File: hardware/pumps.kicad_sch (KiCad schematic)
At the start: 14 parts, among them Q5 BUK6D210

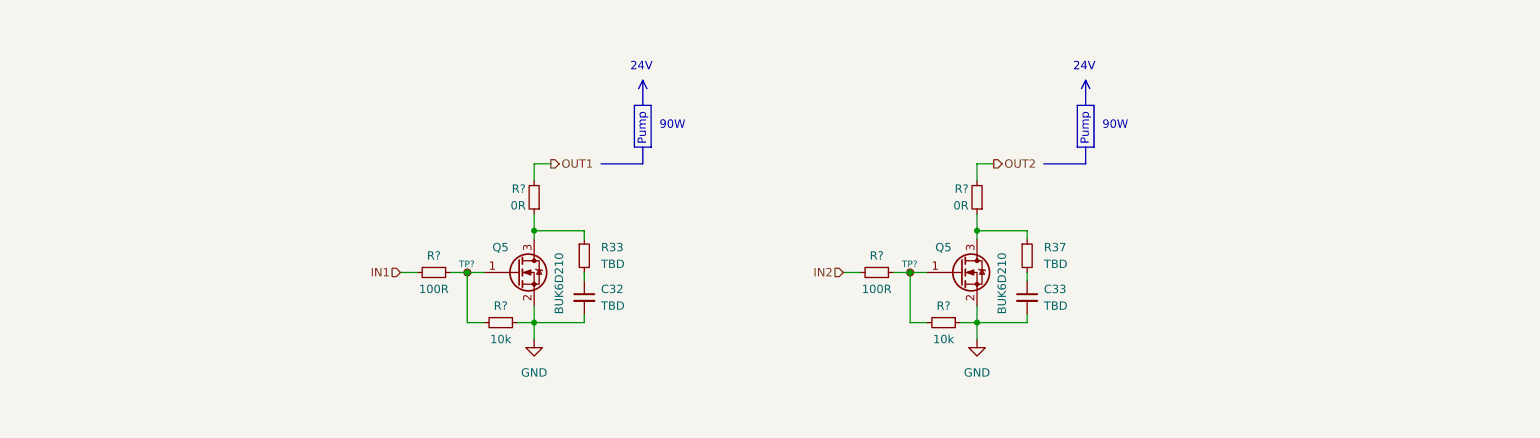
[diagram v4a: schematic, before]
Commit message: Add high-side drivers to the fans and pumps
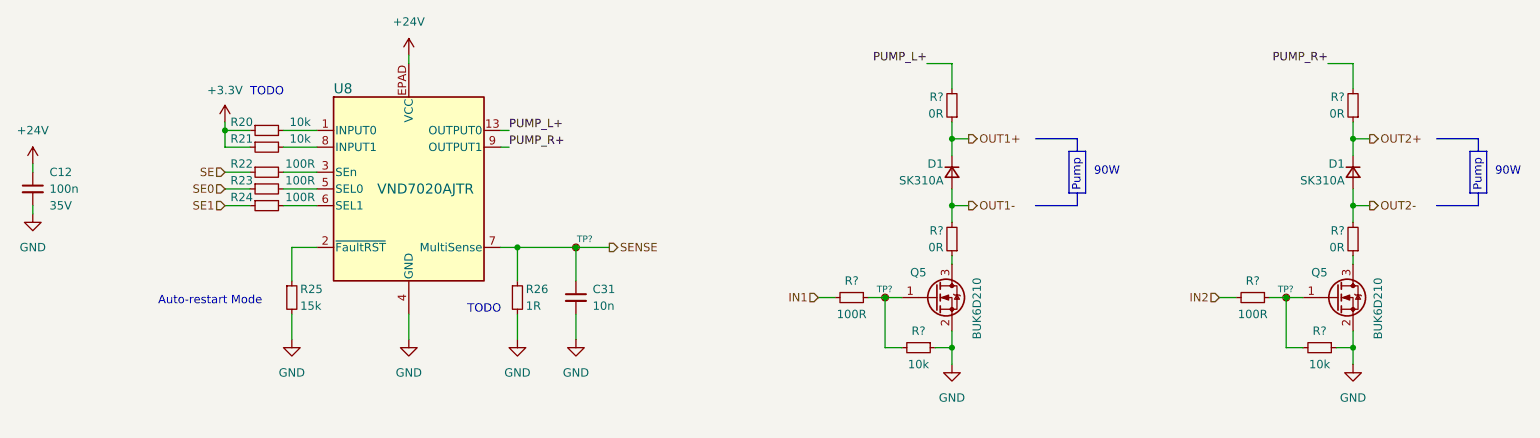
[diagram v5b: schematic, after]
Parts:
- removed C32, C33: TBD, Capacitor_SMD:C_0603_1608Metric, symbol Device:C_Small
- removed Q5 (x2): BUK6D210, Package_DFN_QFN:Diodes_UDFN2020-6_Type-F, symbol Device:Q_NMOS_GSD
- removed R33, R37: TBD, Resistor_SMD:R_0603_1608Metric, symbol Device:R_Small
- removed R? (x2): 0R, Resistor_SMD:R_0603_1608Metric, symbol Device:R_Small
- removed R? (x2): 100R, Resistor_SMD:R_0603_1608Metric, symbol Device:R_Small
- removed R? (x2): 10k, Resistor_SMD:R_0603_1608Metric, symbol Device:R_Small
- removed TP? (x2): TestPoint_Small, TestPoint:TestPoint_Pad_D1.0mm, symbol Connector:TestPoint_Small
- added C12: 100n, Capacitor_SMD:C_0603_1608Metric, symbol Device:C_Small
- added C31: 10n, symbol Device:C_Small
- added D1 (x2): SK310A, Diode_SMD:D_SMA, symbol Device:D_Small
- added Q5 (x2): BUK6D210, Package_DFN_QFN:Diodes_UDFN2020-6_Type-F, symbol Device:Q_NMOS_GSD
- added R20, R21: 10k, symbol Device:R_Small
- added R22, R23, R24: 100R, symbol Device:R_Small
- added R25: 15k, symbol Device:R_Small
- added R26: 1R, symbol Device:R_Small
- added R? (x4): 0R, Resistor_SMD:R_0603_1608Metric, symbol Device:R_Small
- added R? (x2): 100R, Resistor_SMD:R_0603_1608Metric, symbol Device:R_Small
- added R? (x2): 10k, Resistor_SMD:R_0603_1608Metric, symbol Device:R_Small
- added TP? (x3): TestPoint_Small, TestPoint:TestPoint_Pad_D1.0mm, symbol Connector:TestPoint_Small
- added U8: VND7020AJTR, Local_Library:VND7020AJTR, symbol VND7020AJTR:VND7020AJTR
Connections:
- net GND: now also C12.2, C31.2, Q5.2 (S), Q5.2 (S), R25.2, R26.2, R?.1, R?.1, U8.4 (GND)
- net IN1: now also R?.2
- net IN2: now also R?.2
- new net: Q5.1 (G), R?.1, R?.2, TP?.1 (x2)
- new net: Q5.3 (D), R?.1 (x2)
- new net: R21.2, U8.8 (INPUT1)
- new net: R23.2, U8.5 (SEL0)
- new net: R20.2, U8.1 (INPUT0)
- new net: R25.1, U8.2 (~{FaultRST})
- new net: R22.2, U8.3 (SEn)
- new net: R24.2, U8.6 (SEL1)
- new net +24V: C12.1, U8.EPAD (VCC)
- new net +3.3V: R20.1, R21.1
- new net OUT1+: D1.1 (K), R?.1
- new net OUT1-: D1.2 (A), R?.2
- new net OUT2+: D1.1 (K), R?.1
- new net OUT2-: D1.2 (A), R?.2
- new net PUMP_L+: R?.2, U8.13 (OUTPUT0), U8.14 (OUTPUT0), U8.15 (OUTPUT0), U8.16 (OUTPUT0)
- new net PUMP_R+: R?.2, U8.10 (OUTPUT1), U8.11 (OUTPUT1), U8.12 (OUTPUT1), U8.9 (OUTPUT1)
- new net SE: R22.1
- new net SE0: R23.1
- new net SE1: R24.1
- new net SENSE: C31.1, R26.1, TP?.1, U8.7 (MultiSense)
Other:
- note added: "Auto-restart Mode"
- note added: "TODO"
- note removed: "24V"

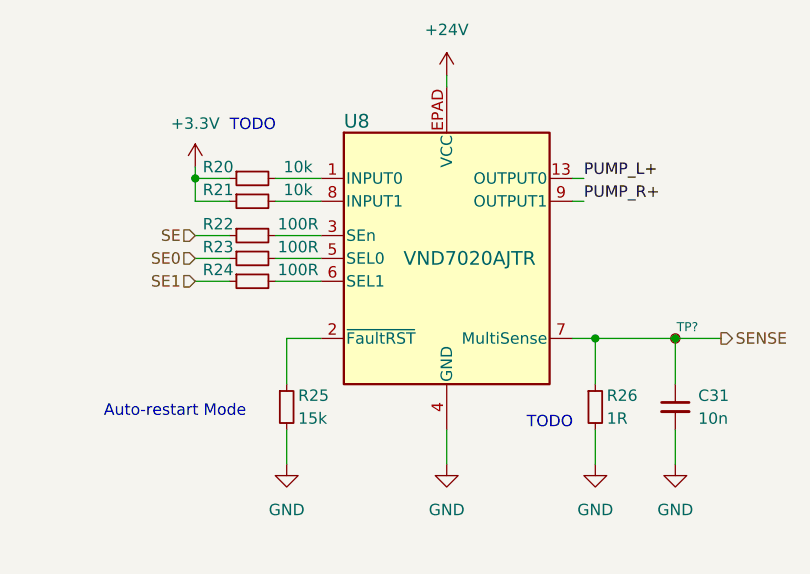
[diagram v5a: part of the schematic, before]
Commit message: Improve the diagram based on the feedback
- add an input LC filter
- remove the USB connector
- add a programmer connector
- move optocouplers into a subsheet
- add a suspension tension meter IC
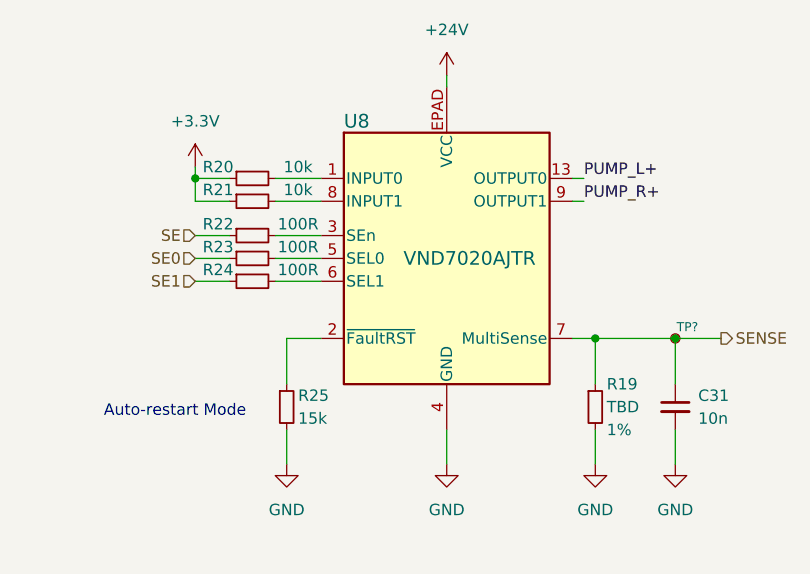
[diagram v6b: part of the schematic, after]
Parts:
- removed R26: 1R, symbol Device:R_Small
- added R19: TBD, Resistor_SMD:R_0603_1608Metric, symbol Device:R_Small
- C12: Rated Voltage (none) -> 35V; Voltage 35V -> (none)
- C31: footprint (none) -> Capacitor_SMD:C_0603_1608Metric
- R20, R21, R22, R23, R24, R25: footprint (none) -> Resistor_SMD:R_0603_1608Metric
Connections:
- net GND: now also R19.2
- net SENSE: now also R19.1
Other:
- note removed: "TODO"
